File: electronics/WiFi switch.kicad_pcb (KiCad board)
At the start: 2 copper layers, 49 x 70 mm, 33 parts, among them J1 Programmer, J2 LOAD, J5 AC IN, K1 RM50-3011-85-1024, Q1 BC817, Q2 BC817, Q3 BC817, SW1 Setup, U2 ESP-12F, U6 DS18S20

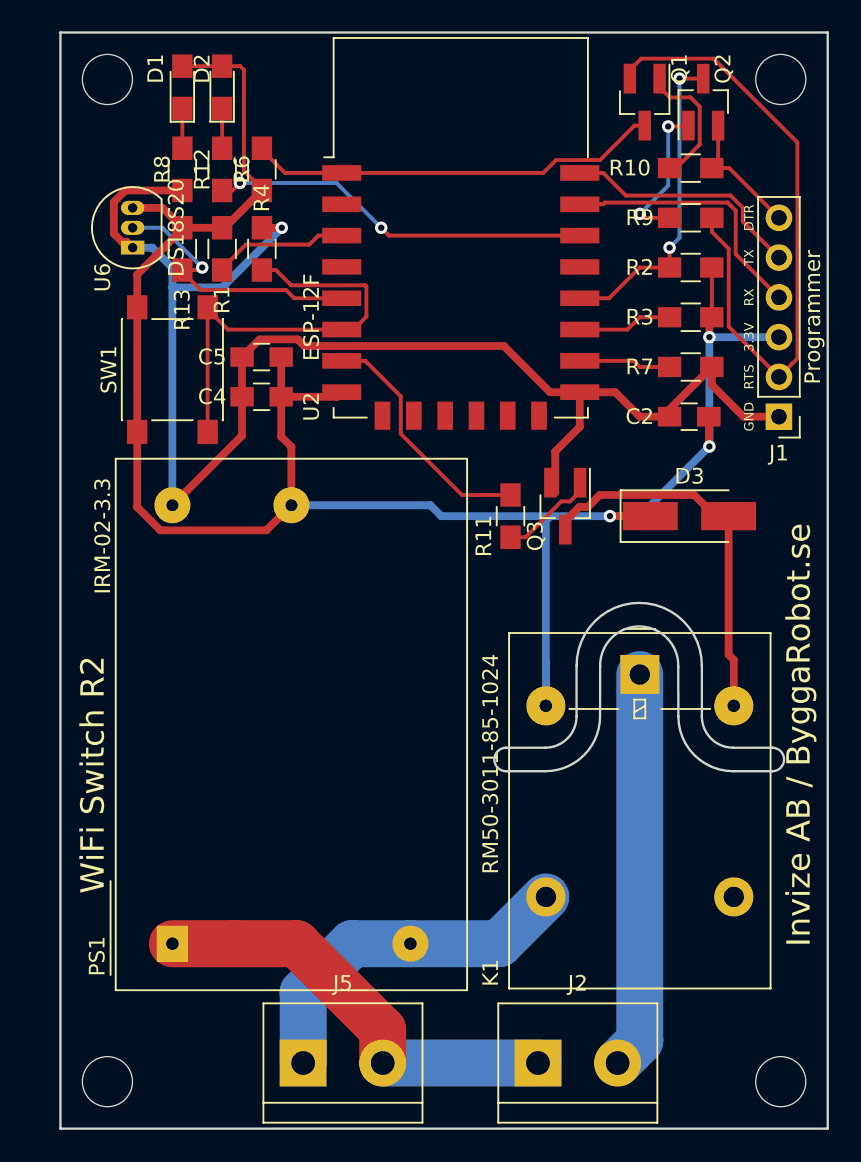
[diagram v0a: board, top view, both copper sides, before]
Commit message: Update PCB for latest schematics changes
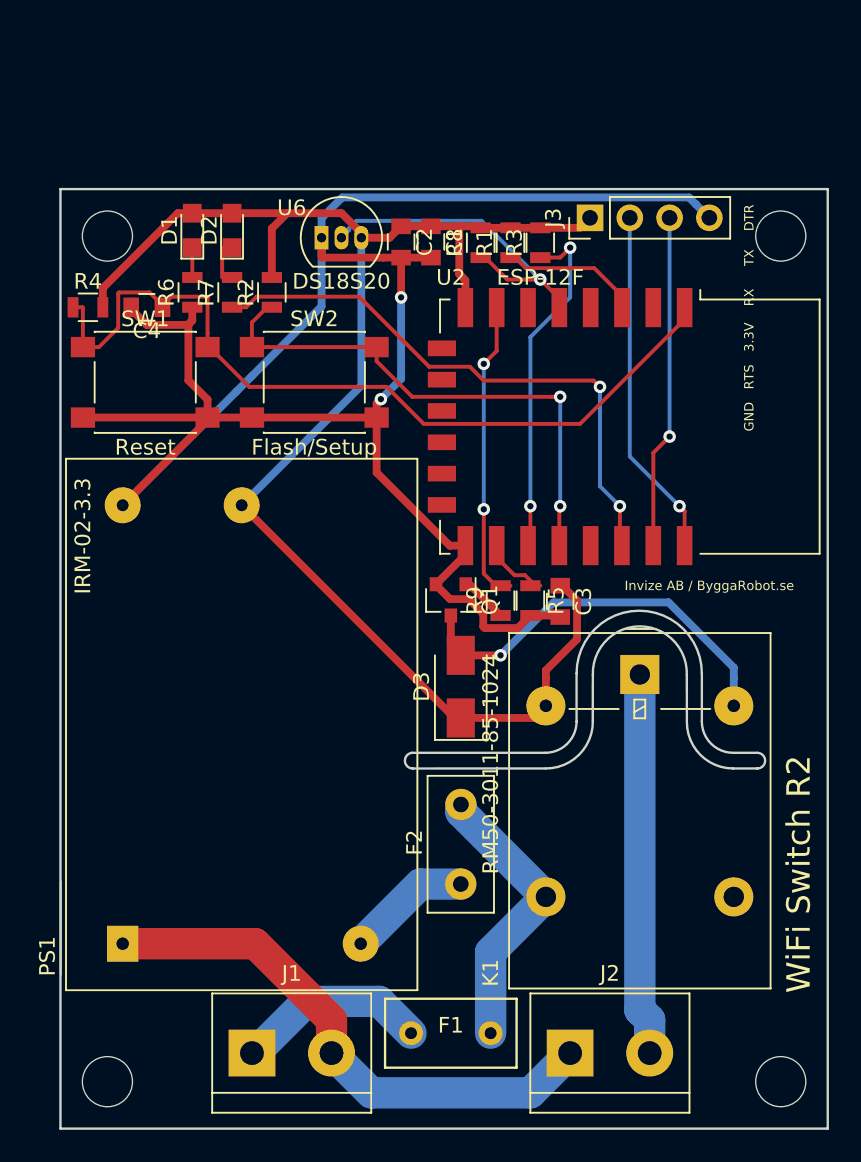
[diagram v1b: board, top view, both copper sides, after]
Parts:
- removed C5: 100nF, Capacitors_SMD:C_0805_HandSoldering
- removed J5: AC IN, Connectors_Terminal_Blocks:TerminalBlock_bornier-2_P5.08mm
- removed Q2, Q3: BC817, TO_SOT_Packages_SMD:SOT-23_Handsoldering
- removed R10, R12: 10K, Resistors_SMD:R_0805_HandSoldering
- removed R11: 1K, Resistors_SMD:R_0805_HandSoldering
- removed R13: 4.7K, Resistors_SMD:R_0805_HandSoldering
- removed the REF** at (223.0, 68.0)
- removed the REF** at (180.0, 68.0)
- added C1: 10uF, Capacitors_SMD:C_0805, F.Cu at (200.7, 78.4)
- added C3: 10uF, Capacitors_SMD:C_0805, F.Cu at (208.9, 101.3)
- added F1: 5A, Fuses:RS Pro Non-resettable fuse, F.Cu at (201.9, 128.9)
- added F2: 0.08A LVR008NK, Fuse_Holders_and_Fuses:Fuse_TE5_Littlefuse-395Series, F.Cu at (202.6, 119.4)
- added J3: Programmer, Pin_Headers:Pin_Header_Straight_1x04_Pitch2.54mm, F.Cu at (210.8, 76.8)
- added R5: 10K, Resistors_SMD:R_0805, F.Cu at (207.0, 101.3)
- added REF**: , Mounting_Holes:MountingHole_3.2mm_M3_ISO14580, F.Cu at (223.0, 78.0)
- added REF**: , Mounting_Holes:MountingHole_3.2mm_M3_ISO14580, F.Cu at (180.0, 78.0)
- added SW2: Flash/Setup, Buttons_Switches_SMD:SW_SPST_PTS645, F.Cu at (193.2, 87.3)
- C2, C4: value 10uF -> 100nF; footprint Capacitors_SMD:C_0805_HandSoldering -> Capacitors_SMD:C_0805
- D1, D2: footprint LEDs:LED_0805_HandSoldering -> LEDs:LED_0805
- D3: footprint Diodes_SMD:D_SMA_Handsoldering -> Diodes_SMD:D_SMA
- J1: value Programmer -> AC IN; footprint Pin_Headers:Pin_Header_Straight_1x06_Pitch2.54mm -> Connectors_Terminal_Blocks:TerminalBlock_bornier-2_P5.08mm
- Q1: footprint TO_SOT_Packages_SMD:SOT-23_Handsoldering -> TO_SOT_Packages_SMD:SOT-23
- R1, R2, R3, R4, R6, R7: footprint Resistors_SMD:R_0805_HandSoldering -> Resistors_SMD:R_0805
- R8: value 10K -> 4.7K; footprint Resistors_SMD:R_0805_HandSoldering -> Resistors_SMD:R_0805
- R9: value 10K -> 1K; footprint Resistors_SMD:R_0805_HandSoldering -> Resistors_SMD:R_0805
- SW1: value Setup -> Reset
- moved J1 52.8 mm to (189.2, 130.2), turned to 0 degrees
- moved Q1 34.1 mm to (201.9, 101.2)
- moved R7 29.7 mm to (188.0, 81.6), turned to 90 degrees
- moved R9 27.3 mm to (205.1, 101.3), turned to 90 degrees
- moved R2 26.8 mm to (190.5, 81.6), turned to 90 degrees
- moved C2 21.5 mm to (198.8, 78.4), turned to 270 degrees
- moved R8 19.6 mm to (203.8, 78.4)
- moved R1 18.4 mm to (205.7, 78.4)
- moved D3 18.2 mm to (202.6, 106.8), turned to 90 degrees
- moved U2 16.7 mm to (213.4, 90.2), turned to 270 degrees
- moved U6 12.1 mm to (193.7, 78.1), turned to 0 degrees
- moved R4 11.7 mm to (178.8, 82.5), turned to 0 degrees
- moved R3 10.7 mm to (207.6, 78.4), turned to 90 degrees
- moved C4 9.29 mm to (182.5, 82.5)
- moved D2 9.16 mm to (188.0, 77.6)
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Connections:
- C4 pad 1: +3V3 -> RST
- J1 pad 1: GND -> Net-(F1-Pad2)
- J1 pad 2: /RTS -> AC-N
- PS1 pad 2: AC-L -> Net-(F2-Pad1)
- Q1 pad 2: /RTS -> GND
- Q1 pad 3: RST -> Net-(D3-Pad2)
- R4 pad 1: GND -> RST
- R4 pad 2: D6 -> +3V3
- R6 pad 1: RST -> GND
- R6 pad 2: +3V3 -> Net-(D1-Pad1)
- R7 pad 1: D8 -> D1
- R7 pad 2: GND -> Net-(D2-Pad1)
- R8 pad 1: GND -> D5
- R8 pad 2: Net-(D1-Pad1) -> +3V3
- R9 pad 1: Net-(Q2-Pad1) -> Net-(Q1-Pad1)
- R9 pad 2: /RTS -> D7
- SW1 pad 1: +3V3 -> RST
- SW1 pad 2: D6 -> GND
- U2 pad 6: D6 -> (no net)
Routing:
- net /RTS: track 41.2 -> 0.00 mm
- net GND: track 95.1 -> 131.7 mm, vias 1 -> 2
- net +3V3: track 130.2 -> 100.3 mm, vias 3 -> 0
- net D6: track 28.1 -> 0.00 mm
- net RST: track 26.4 -> 53.7 mm
- net D4: track 6.06 -> 22.3 mm, vias 0 -> 2
- net D3: track 20.4 -> 34.3 mm
- net D1: track 24.4 -> 36.9 mm
- net Net-(F1-Pad2): track 0.00 -> 12.4 mm
- net Net-(Q2-Pad1): track 9.73 -> 0.00 mm, vias 2 -> 0
- net /DTR: track 8.70 -> 0.00 mm
- net Net-(F2-Pad1): track 0.00 -> 7.97 mm
- net AC-N: track 27.7 -> 34.8 mm
- net TX: track 15.5 -> 22.4 mm, vias 0 -> 1
- net Net-(Q3-Pad1): track 6.21 -> 0.00 mm
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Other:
- board size 49 x 70 mm -> 49 x 60 mm
- net class High voltage: clearance 1 -> 0.8; trace_width 3 -> 2

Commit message: Fix front silk screen layout
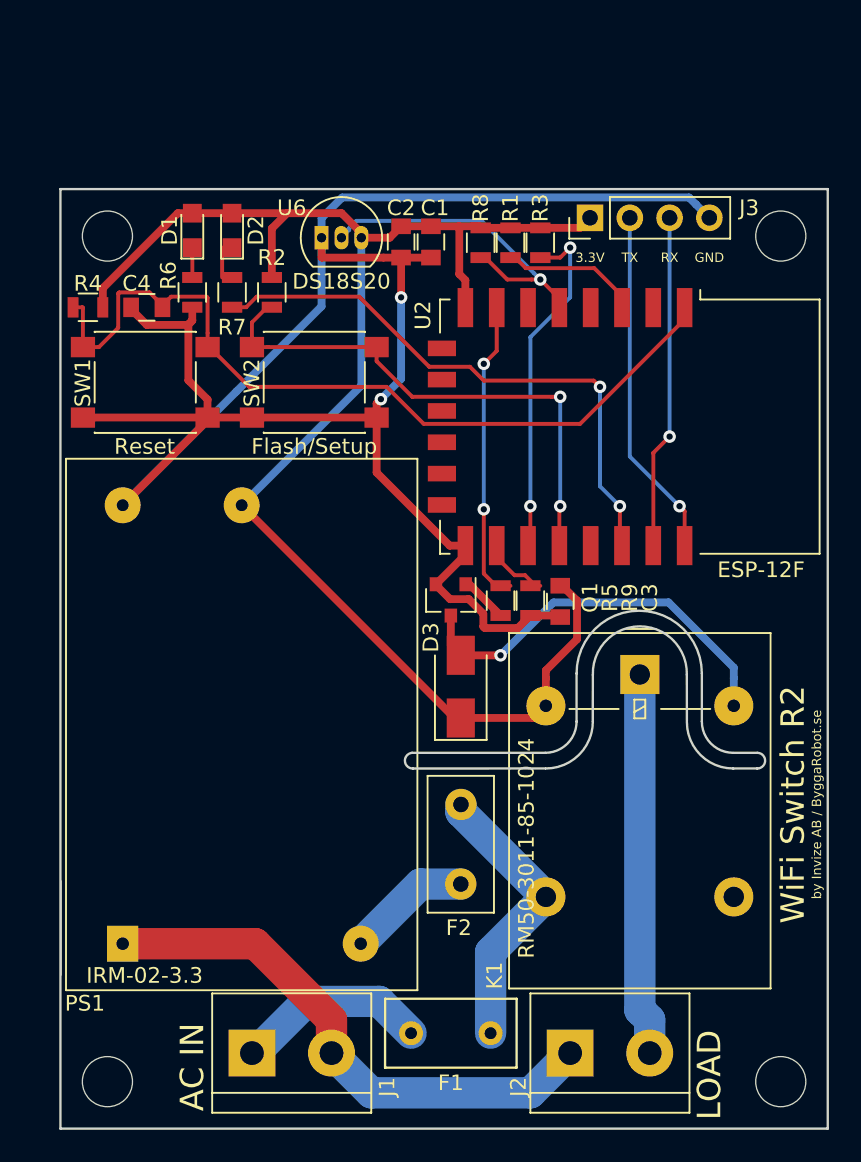
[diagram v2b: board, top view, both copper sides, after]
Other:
- board text added: "AC IN"
- board text added: "LOAD"
- board text added: "by Invize AB / ByggaRobot.se"
- board text removed: "DTR"
- board text removed: "Invize AB / ByggaRobot.se"
- board text removed: "RTS"
